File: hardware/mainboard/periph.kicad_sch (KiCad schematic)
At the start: 87 parts, among them J1 Micro_SD_Card_Det, P1 M2_SOCKET_E, Q1 BSS138, Q2 BSS138, Q3 BSS138, Q5 BSS138, Q7 BSS138, SW2 SW_Push, SW3 SW_Push, SW4 SW_Push, SW5 SW_Push, SW6 SW_Push, U10 MMC5983MA, U11 Si52112-B, U21 74LVC2T45DC, U8 TXS02612, U9 ICM-20789, Y1 25MHz

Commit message: 3d models etc
Signed-off-by: gatecat <gatecat@ds0.me>
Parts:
- SW2, SW3, SW4, SW5, SW6: footprint Button_Switch_SMD:SW_SPST_B3S-1000 -> Button_Switch_SMD:SW_SPST_PTS810
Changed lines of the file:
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@@
       (effects (font (size 1.27 1.27)))
     )
-    (property "Footprint" "Button_Switch_SMD:SW_SPST_B3S-1000" (at 252.73 185.42 0)
+    (property "Footprint" "Button_Switch_SMD:SW_SPST_PTS810" (at 252.73 185.42 0)
       (effects (font (size 1.27 1.27)) hide)
     )
@@
       (effects (font (size 1.27 1.27)))
     )
-    (property "Footprint" "Button_Switch_SMD:SW_SPST_B3S-1000" (at 271.78 220.98 0)
+    (property "Footprint" "Button_Switch_SMD:SW_SPST_PTS810" (at 271.78 220.98 0)
       (effects (font (size 1.27 1.27)) hide)
     )
@@
       (effects (font (size 1.27 1.27)))
     )
-    (property "Footprint" "Button_Switch_SMD:SW_SPST_B3S-1000" (at 271.78 241.3 0)
+    (property "Footprint" "Button_Switch_SMD:SW_SPST_PTS810" (at 271.78 241.3 0)
       (effects (font (size 1.27 1.27)) hide)
     )
@@
       (effects (font (size 1.27 1.27)))
     )
-    (property "Footprint" "Button_Switch_SMD:SW_SPST_B3S-1000" (at 271.78 251.46 0)
+    (property "Footprint" "Button_Switch_SMD:SW_SPST_PTS810" (at 271.78 251.46 0)
       (effects (font (size 1.27 1.27)) hide)
     )
@@
       (effects (font (size 1.27 1.27)))
     )
-    (property "Footprint" "Button_Switch_SMD:SW_SPST_B3S-1000" (at 271.78 231.14 0)
-      (effects (font (size 1.27 1.27)) hide)
-    )
+    (property "Footprint" "Button_Switch_SMD:SW_SPST_PTS810" (at 271.78 231.14 0)
+      (effects (font (size 1.27 1.27)) hide)
+    )

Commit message: Misc tweaks
Signed-off-by: gatecat <gatecat@ds0.me>
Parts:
- R20, R27, R31: value 2.2k -> 10k
- R32, R33, R40, R48, R67, R68, R70, R71, R73, R95: value 1k -> 2.2k
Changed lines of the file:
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@@
       (effects (font (size 1.27 1.27)))
     )
-    (property "Value" "1k" (at 167.64 259.08 90)
+    (property "Value" "2.2k" (at 167.64 259.08 90)
       (effects (font (size 1.27 1.27)))
     )
@@
       (effects (font (size 1.27 1.27)))
     )
-    (property "Value" "1k" (at 91.44 259.08 90)
+    (property "Value" "2.2k" (at 91.44 259.08 90)
       (effects (font (size 1.27 1.27)))
     )
@@
       (effects (font (size 1.27 1.27)))
     )
-    (property "Value" "1k" (at 138.43 259.08 90)
+    (property "Value" "2.2k" (at 138.43 259.08 90)
       (effects (font (size 1.27 1.27)))
     )
@@
       (effects (font (size 1.27 1.27)))
     )
-    (property "Value" "1k" (at 114.3 259.08 90)
+    (property "Value" "2.2k" (at 114.3 259.08 90)
       (effects (font (size 1.27 1.27)))
     )
@@
       (effects (font (size 1.27 1.27)))
     )
-    (property "Value" "1k" (at 96.52 259.08 90)
+    (property "Value" "2.2k" (at 96.52 259.08 90)
       (effects (font (size 1.27 1.27)))
     )
@@
       (effects (font (size 1.27 1.27)))
     )
-    (property "Value" "1k" (at 191.77 259.08 90)
+    (property "Value" "2.2k" (at 191.77 259.08 90)
       (effects (font (size 1.27 1.27)))
     )
@@
       (effects (font (size 1.27 1.27)))
     )
-    (property "Value" "1k" (at 119.38 259.08 90)
+    (property "Value" "2.2k" (at 119.38 259.08 90)
       (effects (font (size 1.27 1.27)))
     )
@@
       (effects (font (size 1.27 1.27)))
     )
-    (property "Value" "1k" (at 186.69 259.08 90)
+    (property "Value" "2.2k" (at 186.69 259.08 90)
       (effects (font (size 1.27 1.27)))
     )
@@
       (effects (font (size 1.27 1.27)))
     )
-    (property "Value" "1k" (at 143.51 259.08 90)
+    (property "Value" "2.2k" (at 143.51 259.08 90)
       (effects (font (size 1.27 1.27)))
     )
@@
       (effects (font (size 1.27 1.27)))
     )
-    (property "Value" "2.2k" (at 88.242 187.96 90)
+    (property "Value" "10k" (at 88.242 187.96 90)
       (effects (font (size 1.27 1.27)))
     )
@@
       (effects (font (size 1.27 1.27)))
     )
-    (property "Value" "1k" (at 162.56 259.08 90)
+    (property "Value" "2.2k" (at 162.56 259.08 90)
       (effects (font (size 1.27 1.27)))
     )
@@
       (effects (font (size 1.27 1.27)))
     )
-    (property "Value" "2.2k" (at 47.602 187.96 90)
+    (property "Value" "10k" (at 47.602 187.96 90)
       (effects (font (size 1.27 1.27)))
     )
@@
       (effects (font (size 1.27 1.27)))
     )
-    (property "Value" "2.2k" (at 130.152 187.96 90)
+    (property "Value" "10k" (at 130.152 187.96 90)
       (effects (font (size 1.27 1.27)))
     )

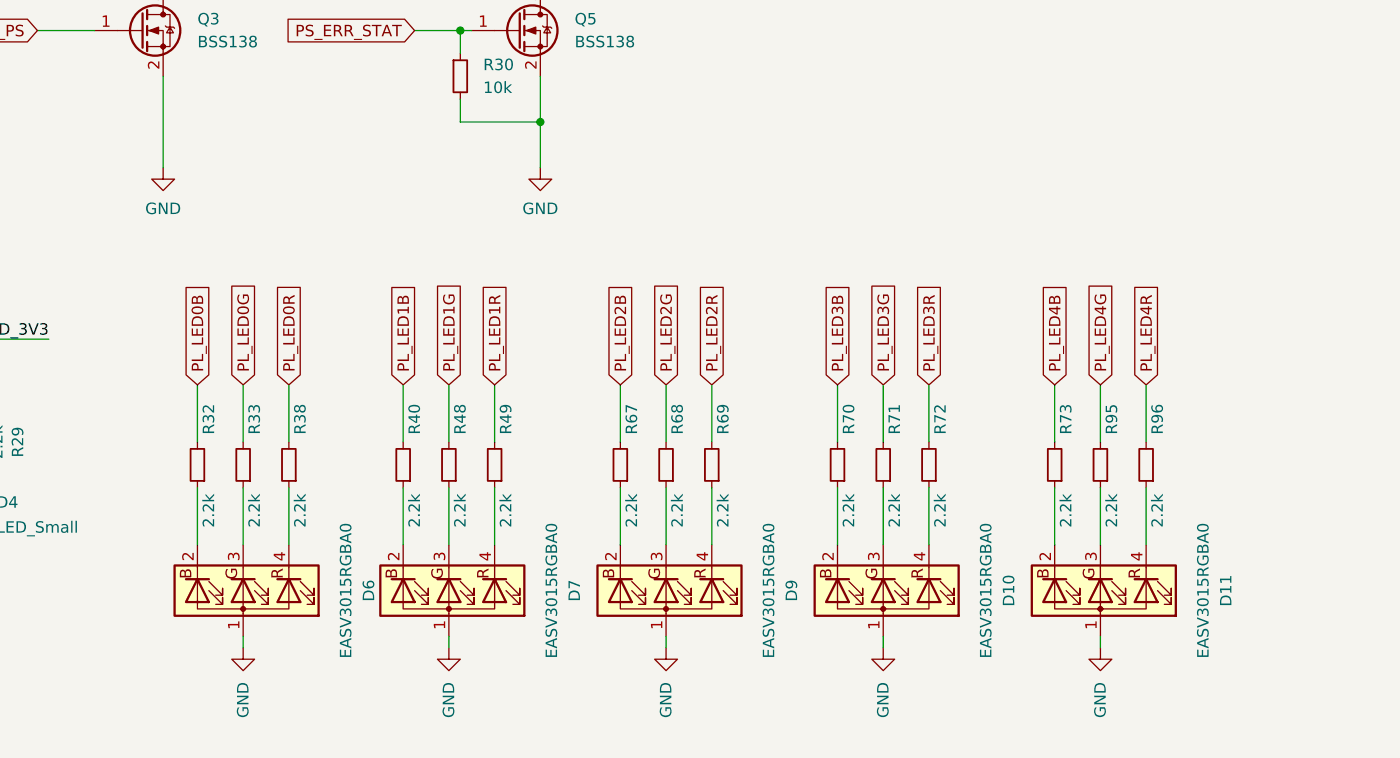
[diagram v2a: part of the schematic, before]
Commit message: hardware: LED associated DFM improvement
Signed-off-by: gatecat <gatecat@ds0.me>
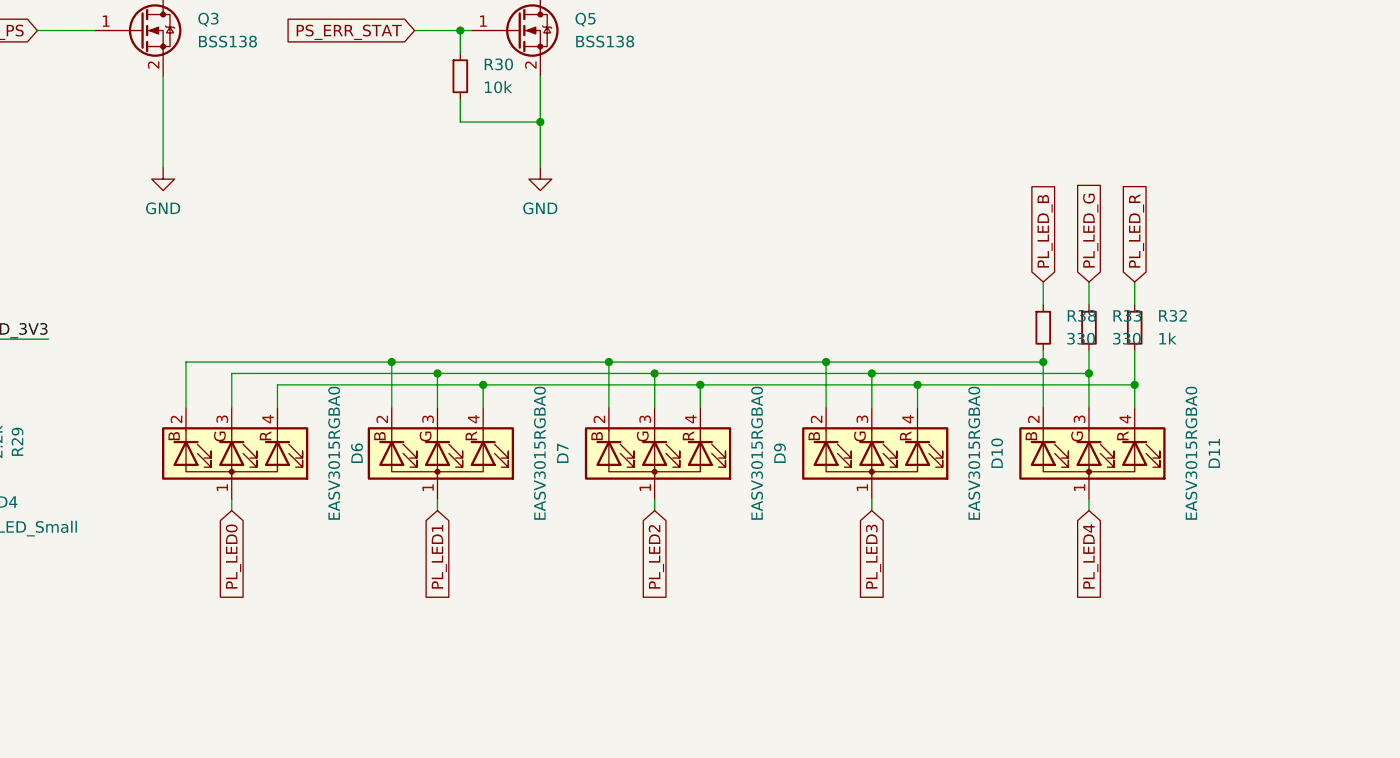
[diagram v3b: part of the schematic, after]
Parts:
- removed R40, R48, R49, R67, R68, R69, R70, R71, R72, R73, R95, R96: 2.2k, Resistor_SMD:R_0402_1005Metric, symbol Device:R_Small
- R32: value 2.2k -> 1k
- R33, R38: value 2.2k -> 330
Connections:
- net PL_LED0B is gone; now on an unnamed net: R32.2
- net PL_LED0G is gone; now on an unnamed net: R33.2
- net PL_LED0R is gone; now on an unnamed net: R38.2
- net GND: no longer D10.1 (A), D11.1 (A), D6.1 (A), D7.1 (A), D9.1 (A)
- net at D10.3 (GK): now also D11.3 (GK), D6.3 (GK), D7.3 (GK), D9.3 (GK)
- net at D7.4 (RK): now also D10.4 (RK), D11.4 (RK), D6.4 (RK), D9.4 (RK)
- net at D6.2 (BK): now also D10.2 (BK), D11.2 (BK), D7.2 (BK), D9.2 (BK); no longer R32.1
- net PL_LED_G: now reaches R33.1
- net PL_LED_G: no longer D6.3 (GK)
- net PL_LED_B: now reaches R38.1
- net PL_LED_B: no longer D6.4 (RK)
- new net PL_LED0: D6.1 (A)
- new net PL_LED1: D7.1 (A)
- new net PL_LED2: D9.1 (A)
- new net PL_LED3: D10.1 (A)
- new net PL_LED4: D11.1 (A)
- new net PL_LED_R: R32.1
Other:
- moved on the sheet: D10, D11, D6, D7, D9
